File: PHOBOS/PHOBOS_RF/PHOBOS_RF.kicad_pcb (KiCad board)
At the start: 2 copper layers, 7 parts, among them IC1 PD2328J5050S2HF, J1 RF_IN, J7 Conn_01x05

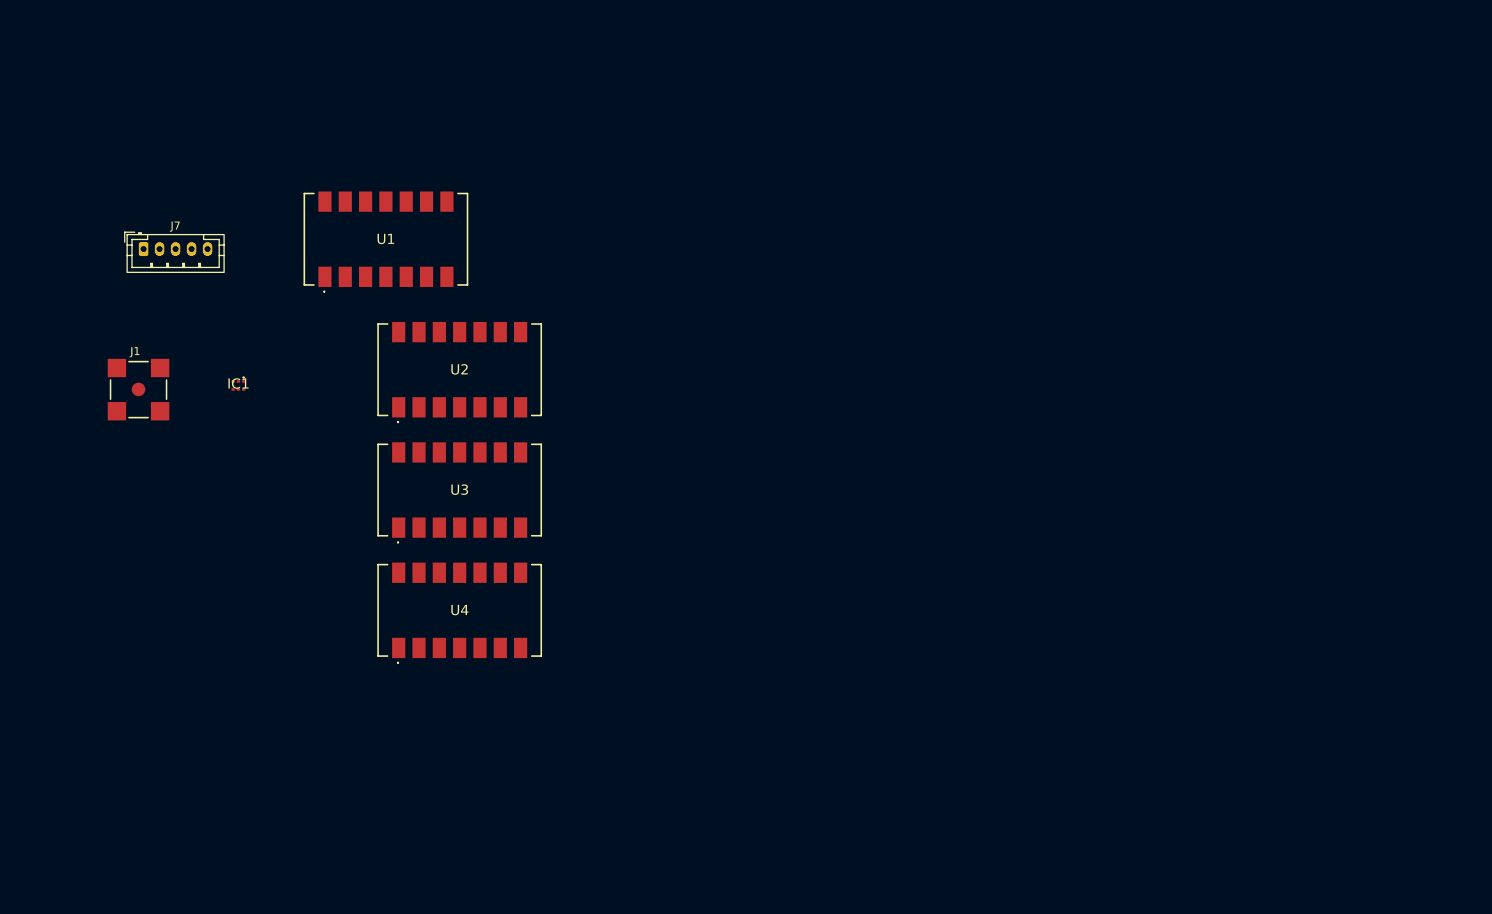
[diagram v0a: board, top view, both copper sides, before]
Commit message: Divider Components added and wired
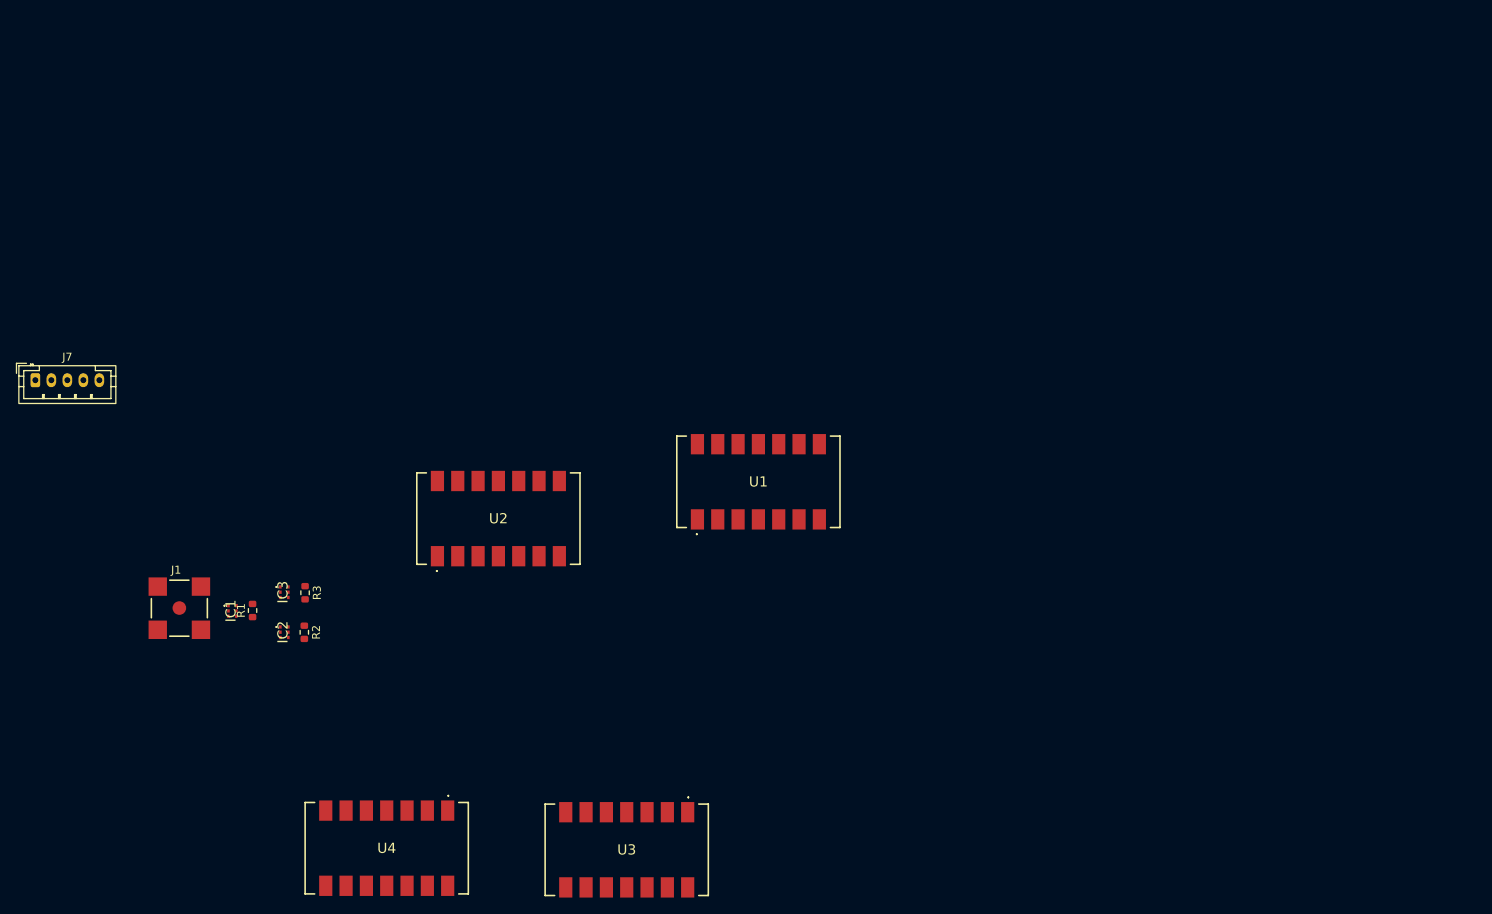
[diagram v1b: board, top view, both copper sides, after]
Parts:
- added IC2: PD2328J5050S2HF, PD2328J5050S2HF:PD2328J5050S2HF, F.Cu at (134.6, 105.0)
- added IC3: PD2328J5050S2HF, PD2328J5050S2HF:PD2328J5050S2HF, F.Cu at (134.6, 100.0)
- added R1: 100, Resistor_SMD:R_0603_1608Metric, F.Cu at (130.7, 102.3)
- added R2: 100, Resistor_SMD:R_0603_1608Metric, F.Cu at (137.1, 105.0)
- added R3: 100, Resistor_SMD:R_0603_1608Metric, F.Cu at (137.2, 100.1)
- moved U1 55.6 mm to (193.9, 86.2)
- moved U3 49.6 mm to (177.4, 132.2), turned to 180 degrees
- moved U4 31.1 mm to (147.4, 132.0), turned to 180 degrees
- moved IC1 28.2 mm to (128.1, 102.3), turned to 90 degrees
- moved J1 27.8 mm to (121.5, 102.0)
- moved J7 21.3 mm to (103.5, 73.5)
- moved U2 19.2 mm to (161.4, 90.8)
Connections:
- IC1 pad 1: unconnected-(IC1-GND_1-Pad1) -> GND
- IC1 pad 2: unconnected-(IC1-INPUT-Pad2) -> /RF_IN
- IC1 pad 3: unconnected-(IC1-GND_2-Pad3) -> GND
- IC1 pad 4: unconnected-(IC1-OUTPUT1-Pad4) -> Net-(IC1-OUTPUT1)
- IC1 pad 5: unconnected-(IC1-GND_3-Pad5) -> GND
- IC1 pad 6: unconnected-(IC1-OUTPUT2-Pad6) -> Net-(IC1-OUTPUT2)
- U1 pad 1: /RF_IN -> Net-(IC2-OUTPUT1)
- U2 pad 1: /RF_IN -> Net-(IC2-OUTPUT2)
- U3 pad 1: /RF_IN -> Net-(IC3-OUTPUT1)
- U4 pad 1: /RF_IN -> Net-(IC3-OUTPUT2)

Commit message: initial layout
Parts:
- moved U2 68.0 mm to (222.9, 119.8), turned to 180 degrees
- moved U4 64.3 mm to (160.5, 69.0)
- moved U3 64.3 mm to (190.5, 69.2)
- moved U1 46.4 mm to (158.9, 116.7)
- moved R2 25.0 mm to (141.0, 129.7)
- moved IC2 25.0 mm to (138.5, 129.7)
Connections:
- net Net-(IC1-OUTPUT1) renamed /S1_OUT1
- net Net-(IC1-OUTPUT2) renamed /S1_OUT2
- net Net-(IC2-OUTPUT1) renamed /P1
- net Net-(IC2-OUTPUT2) renamed /P2
- net Net-(IC3-OUTPUT1) renamed /P3
- net Net-(IC3-OUTPUT2) renamed /P4
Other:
- board outline added: 167 x 107.5 mm
